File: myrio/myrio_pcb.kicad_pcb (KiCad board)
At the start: 4 copper layers, 220 x 93.5 mm, 143 parts, among them J1 CONN_02X03, J2 CONN_02X03, J3 CONN_02X03, J4 CONN_02X03, P1 CONN_02X17, P2 CONN_02X17, Q1 PN2222A, Q10 PN2222A, Q11 PN2222A, Q12 PN2222A, Q13 PN2222A, Q14 PN2222A, Q15 PN2222A, Q16 PN2222A, Q17 PN2222A, Q18 PN2222A, Q19 PN2222A, Q2 PN2222A, Q20 PN2222A, Q3 PN2222A, Q4 PN2222A, Q5 PN2222A, Q6 PN2222A, Q7 PN2222A, Q8 PN2222A, Q9 PN2222A, T1 Phoenix_Contact_1935187, T2 Phoenix_Contact_1935187, T3 Phoenix_Contact_1935187, T4 Phoenix_Contact_1935187, T5 Phoenix_Contact_1935187, U1 stacked-DB9, U10 INA219, U11 INA219, U13 INA219, U14 stacked-rj45-LED, U15 stacked-rj45-LED, U2 stacked-DB9, U3 stacked-rj45-LED, U4 stacked-rj45-LED, U5 stacked-rj45-LED, U6 BNO055, U7 stacked-rj45-LED, U8 stacked-DB9

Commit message: done for real this time
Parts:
- removed C8: C, Capacitors_THT:CP_Radial_D5.0mm_P2.50mm
- removed D21: D, Diodes_THT:D_DO-35_SOD27_P5.08mm_Vertical_AnodeUp
- removed R34: R, Resistors_THT:R_Axial_DIN0204_L3.6mm_D1.6mm_P5.08mm_Horizontal
- removed the REF** at (23.7, 48.1)
- removed the REF** at (23.7, 105.6)
- removed the REF** at (234.7, 105.6)
- removed T5: Phoenix_Contact_1935187, footprints:Phoenix_Contact_1935187
- added REF**: 1pin, Connectors:1pin, F.Cu at (23.5, 47.9)
- added REF**: 1pin, Connectors:1pin, F.Cu at (23.5, 105.6)
- added REF**: 1pin, Connectors:1pin, F.Cu at (234.5, 105.6)
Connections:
- RE8 pad 5: SolenoidPower -> 24V_activation
- RE8 pad 6: SolenoidPower -> 24V_activation
- U14 pad 11: SolenoidGround -> DGND
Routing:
- net SolenoidPower: track 242.5 -> 0.00 mm, vias 4 -> 0
- net SolenoidGround: track 177.3 -> 0.00 mm, vias 1 -> 0
- net 2way_open_3: track 131.8 -> 62.5 mm, vias 6 -> 5
- net 24V_activation: track 66.8 -> 61.7 mm
- net Net-(C8-Pad2): track 4.71 -> 0.00 mm
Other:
- board text removed: "SLN+"
- board text removed: "SLN-"

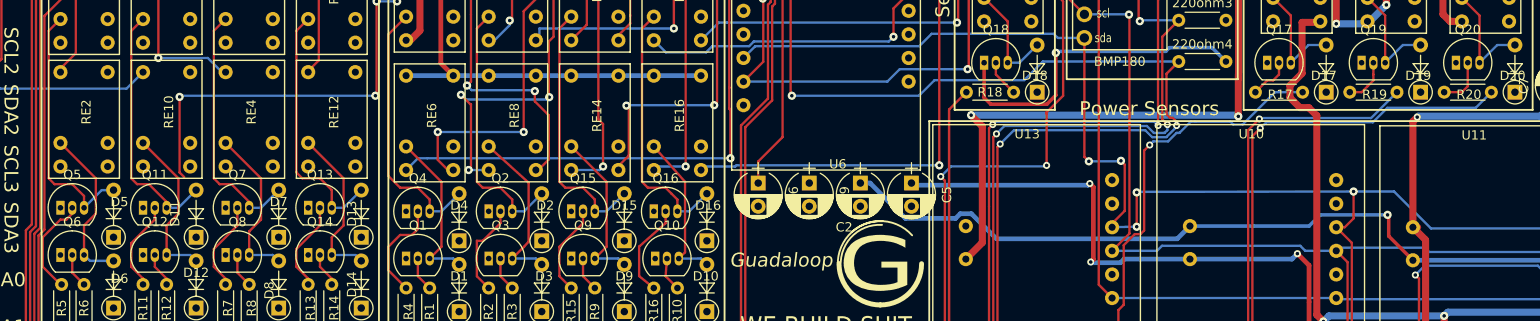
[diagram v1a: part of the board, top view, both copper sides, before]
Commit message: made the anal rings bigger
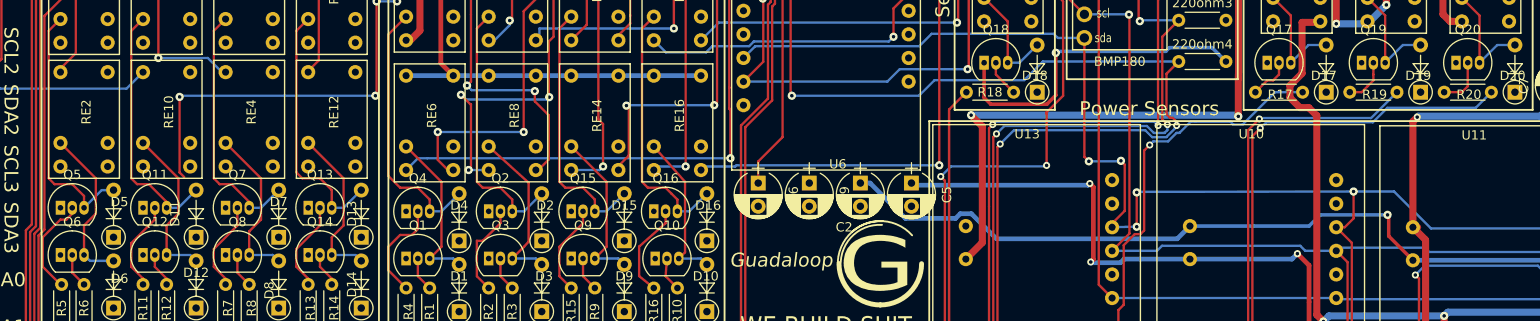
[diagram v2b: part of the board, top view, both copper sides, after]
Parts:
- Q1, Q10, Q11, Q12, Q13, Q14, Q15, Q16, Q17, Q18, Q19, Q2, Q20, Q3, Q4, Q5, Q6, Q7, Q8, Q9: footprint TO_SOT_Packages_THT:TO-92_Inline_Narrow_Oval -> footprints:TO-92_Inline_Narrow_Oval_edit
